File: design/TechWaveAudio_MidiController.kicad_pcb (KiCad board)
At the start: 2 copper layers, 111.5 x 128.5 mm, 92 parts, among them J1 Control, J10 Midi, J12 PiPico2, J13 Velocity, J14 Note, J2 PowerBus, J3 Aux, J4 Gate, J5 Clock, J6 Trigger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

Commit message: working production hardware
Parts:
- moved R25 6.33 mm to (107.9, 37.0)
- moved C11 5.06 mm to (116.8, 41.9), turned to 0 degrees
- moved U6 2.92 mm to (114.1, 40.3)
- moved C8 2.78 mm to (107.8, 44.3), turned to -90 degrees
- moved C10 2.50 mm to (109.5, 42.2)
- moved R24 2.31 mm to (106.7, 37.0), turned to -90 degrees
- moved C9 1.71 mm to (114.6, 44.3), turned to -90 degrees
- moved U5 0.97 mm to (107.0, 40.3)
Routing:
- net GND: track 193.6 -> 214.7 mm, vias 11 -> 8
- net +5V: track 224.6 -> 218.3 mm, vias 4 -> 5
- net /velDAC: track 12.1 -> 15.3 mm
- net /4725Data: track 20.8 -> 22.4 mm
- net /4725Clk: track 23.5 -> 25.0 mm

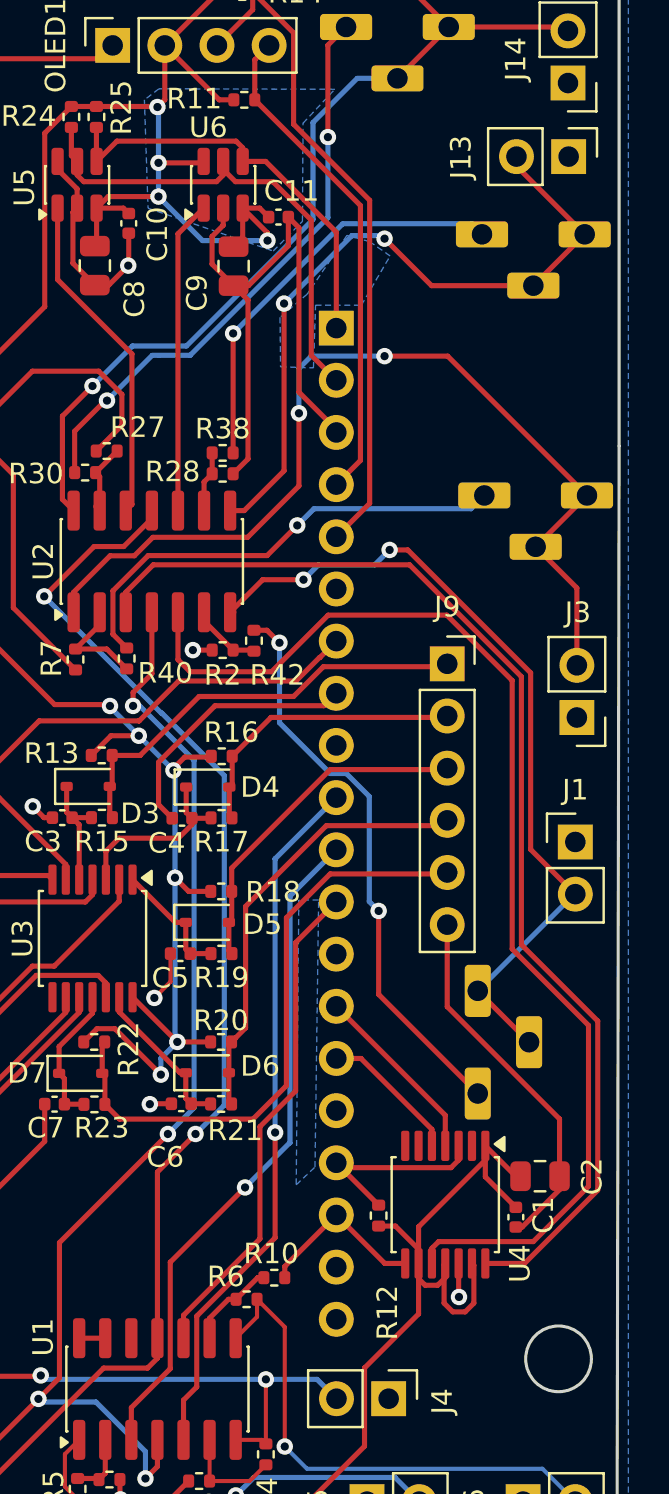
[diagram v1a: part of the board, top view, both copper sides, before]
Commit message: correct i2c / spi
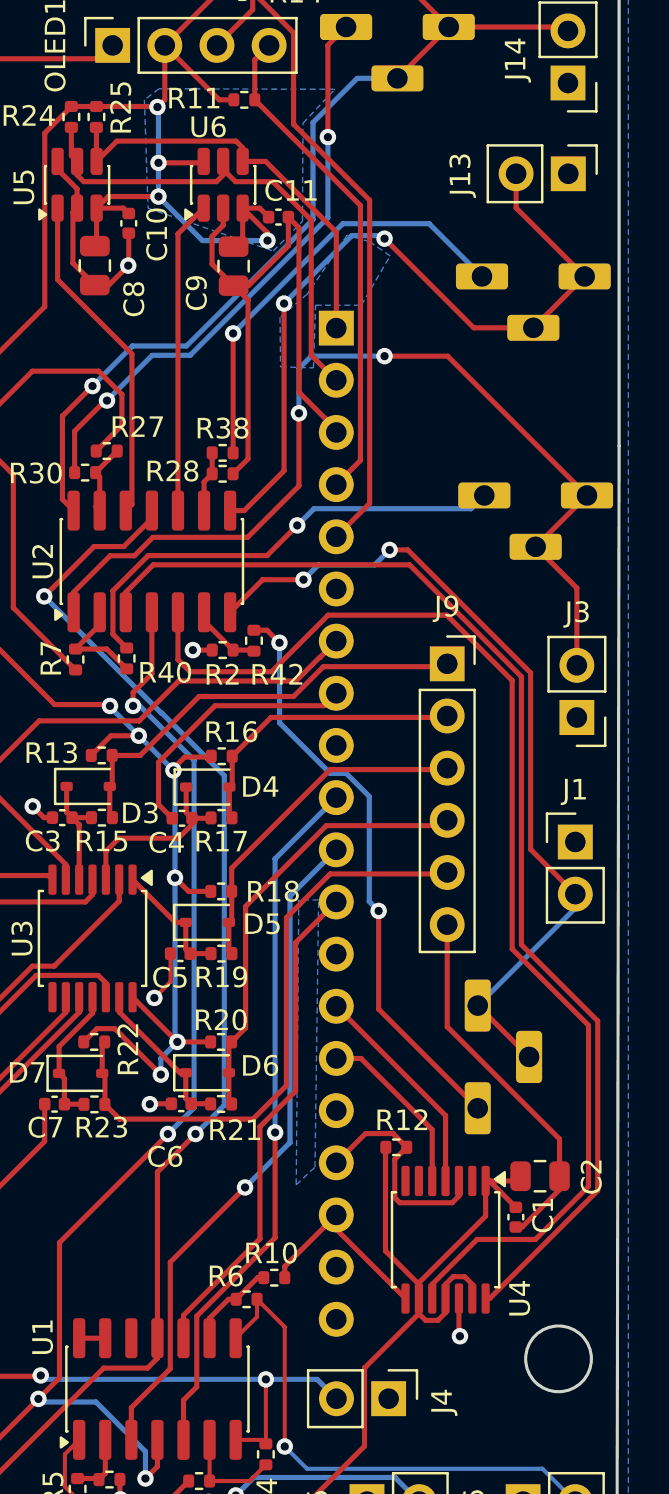
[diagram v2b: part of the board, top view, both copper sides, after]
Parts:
- moved R12 3.43 mm to (122.5, 87.2), turned to 180 degrees
- moved R39 2.05 mm to (129.2, 46.8)
- moved U4 1.71 mm to (124.9, 91.7)
- moved J13 0.84 mm to (130.9, 39.8)
- moved R43 0.72 mm to (128.5, 82.8)
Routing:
- net +5V: track 218.3 -> 216.1 mm
- net /velOut: track 34.8 -> 36.9 mm
- net /4902Clk: track 8.99 -> 10.7 mm
- net /4902Data: track 6.89 -> 8.60 mm
- net /4902CS: track 9.81 -> 11.4 mm
- net GND: track 214.7 -> 216.1 mm
- net Net-(R38-Pad2): track 20.4 -> 21.2 mm
- net /ctlOut: track 40.5 -> 41.2 mm
- net Net-(R42-Pad2): track 27.9 -> 28.7 mm
- net /auxDACOut: track 56.5 -> 57.2 mm
- net /ctlDACOut: track 57.1 -> 57.7 mm

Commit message: working multicore
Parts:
- moved R22 2.15 mm to (109.3, 83.6), turned to -90 degrees
- moved R14 0.39 mm to (114.7, 31.2)
- turned R27 to 180 degrees
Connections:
- SW1 pad 2: unconnected-(SW1-Pad2) -> Net-(D2-A)
- SW1 pad 3: Net-(D2-A) -> unconnected-(SW1-Pad3)
- SW1 pad 6: noteOut -> unconnected-(SW1-Pad6)
- SW1 pad 7: unconnected-(SW1-Pad7) -> noteOut
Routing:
- net GND: track 216.1 -> 260.5 mm, vias 8 -> 4
- net 3.3vSource: track 71.3 -> 67.4 mm
- net +5V: track 216.1 -> 213.4 mm
- net noteOut: track 125.9 -> 123.4 mm, vias 2 -> 1
- net Net-(D2-A): track 16.7 -> 15.7 mm
- net /trgOut: track 25.3 -> 24.6 mm
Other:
- outline, holes or cut-outs redrawn
- board text removed: "DOUBLECHECK"

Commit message: PCB update; cleanups
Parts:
- added C21: 10uF, Capacitor_SMD:C_0805_2012Metric, F.Cu at (110.5, 64.3)
- added C22: 100nf, Capacitor_SMD:C_0402_1005Metric, F.Cu at (107.3, 65.0)
- added C23: 100nf, Capacitor_SMD:C_0402_1005Metric, F.Cu at (112.0, 102.0)
- added C24: 10uF, Capacitor_SMD:C_0805_2012Metric, F.Cu at (111.2, 103.6)
- R37, R39, R41, R43: footprint Resistor_THT:Bourns 3306P-1-102 Trimmer Resistor -> Potentiometer_THT:Potentiometer_Piher_PT-10-V10_Vertical
- moved R37 35.6 mm to (87.7, 41.8), turned to 90 degrees
- moved J5 15.7 mm to (106.0, 108.6), turned to 180 degrees
- moved R39 14.0 mm to (126.3, 33.1), turned to -90 degrees
- moved R41 10.5 mm to (129.9, 47.0), turned to -90 degrees
- moved J6 8.85 mm to (119.8, 104.3)
- moved J4 7.99 mm to (128.4, 104.3), turned to 90 degrees
- moved C2 3.93 mm to (128.8, 92.5)
- moved R43 3.82 mm to (130.3, 79.5), turned to -90 degrees
- moved U4 3.26 mm to (124.2, 94.9)
- moved C1 2.86 mm to (125.5, 89.9), turned to 90 degrees
- moved R12 2.03 mm to (122.4, 89.2)
- moved R8 1.95 mm to (114.2, 102.0)
- moved R5 1.45 mm to (106.9, 102.4)
- moved R4 1.45 mm to (116.1, 100.7)
- moved R10 1.45 mm to (116.5, 92.1)
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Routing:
- net GND: track 260.5 -> 277.8 mm
- net /clkOut: track 21.6 -> 7.03 mm, vias 1 -> 0
- net gateOut: track 42.1 -> 55.8 mm
- net /trgOut: track 24.6 -> 15.1 mm
- net /ctlOut: track 41.2 -> 49.8 mm
- net Net-(R40-Pad2): track 23.1 -> 29.6 mm, vias 1 -> 2
- net +12V: track 97.4 -> 102.5 mm
- net noteOut: track 123.4 -> 119.0 mm
- net /ctlDACOut: track 57.7 -> 62.0 mm
- net /auxDACOut: track 57.2 -> 61.5 mm
- net +5V: track 213.4 -> 209.2 mm
- net Net-(R38-Pad2): track 21.2 -> 25.2 mm, vias 1 -> 2
- net 3.3vSource: track 67.4 -> 70.3 mm, vias 6 -> 7
- net /4902Data: track 8.60 -> 11.5 mm
- net /4902Clk: track 10.7 -> 13.6 mm
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
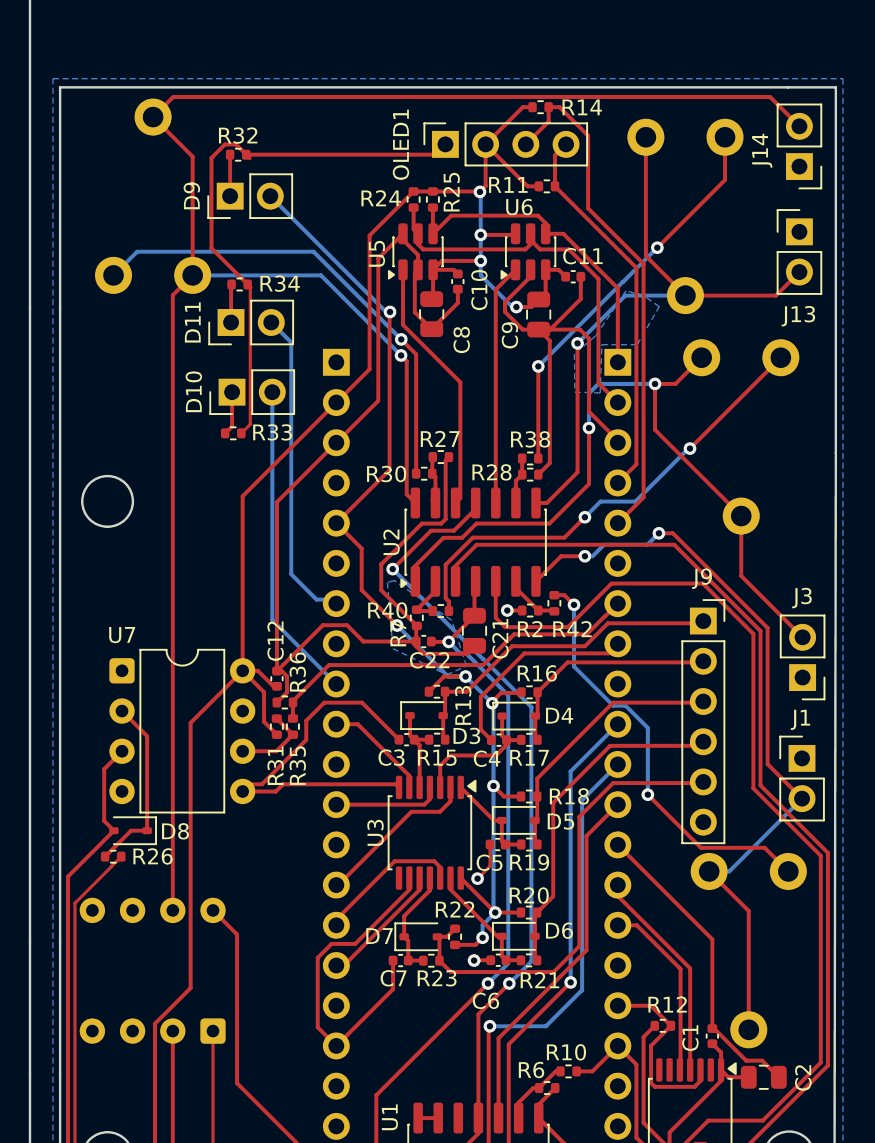
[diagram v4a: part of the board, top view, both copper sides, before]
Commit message: doc cleanups and add images
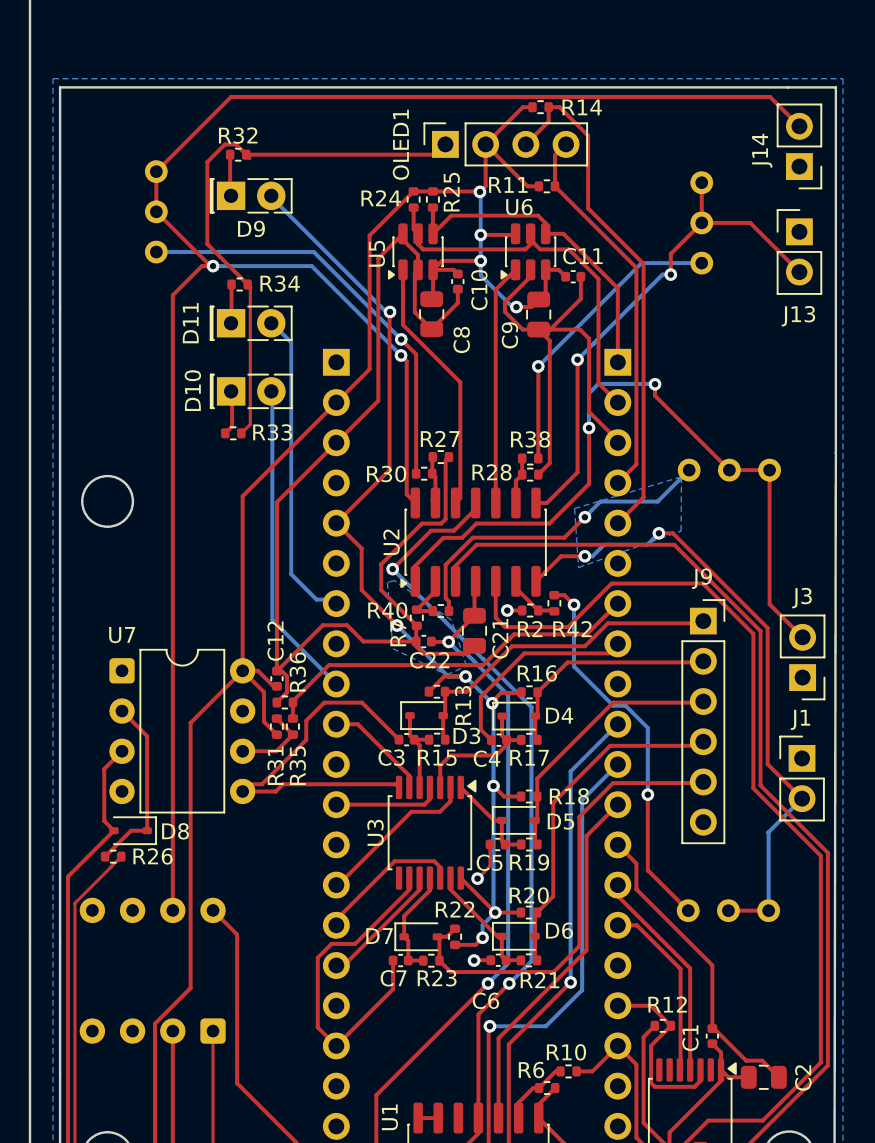
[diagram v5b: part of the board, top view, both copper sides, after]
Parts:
- D10, D11, D9: footprint Connector_PinHeader_2.54mm:PinHeader_1x02_P2.54mm_Vertical -> LED_THT:LED_Rectangular_W5.0mm_H2.0mm
- R37, R39, R41, R43: footprint Potentiometer_THT:Potentiometer_Piher_PT-10-V10_Vertical -> Potentiometer_THT:Potentiometer_Bourns_3296X_Horizontal
- moved R41 9.16 mm to (124.1, 54.1), turned to 180 degrees
- moved R39 8.08 mm to (124.9, 41.0)
- moved R43 6.79 mm to (124.0, 82.0), turned to 180 degrees
- moved R37 3.08 mm to (90.4, 40.4), turned to -90 degrees
- moved D10 0.08 mm to (95.2, 49.1), turned to 0 degrees
- moved D9 0.06 mm to (95.2, 36.8), turned to 0 degrees
- moved D11 0.05 mm to (95.2, 44.9), turned to 0 degrees
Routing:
- net Net-(R40-Pad2): track 29.6 -> 20.9 mm, vias 2 -> 1
- net /ctlOut: track 49.8 -> 41.5 mm
- net Net-(R38-Pad2): track 25.2 -> 18.8 mm, vias 2 -> 1
- net /velOut: track 38.5 -> 32.7 mm, vias 1 -> 2
- net Net-(R30-Pad2): track 30.0 -> 26.7 mm
- net Net-(R42-Pad2): track 26.8 -> 24.3 mm
- net /auxOut: track 47.7 -> 45.6 mm
- net noteOut: track 119.0 -> 117.2 mm, vias 1 -> 2
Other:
- board text added: "v. 1.1.0"
- board text removed: "v. 1.0.0"

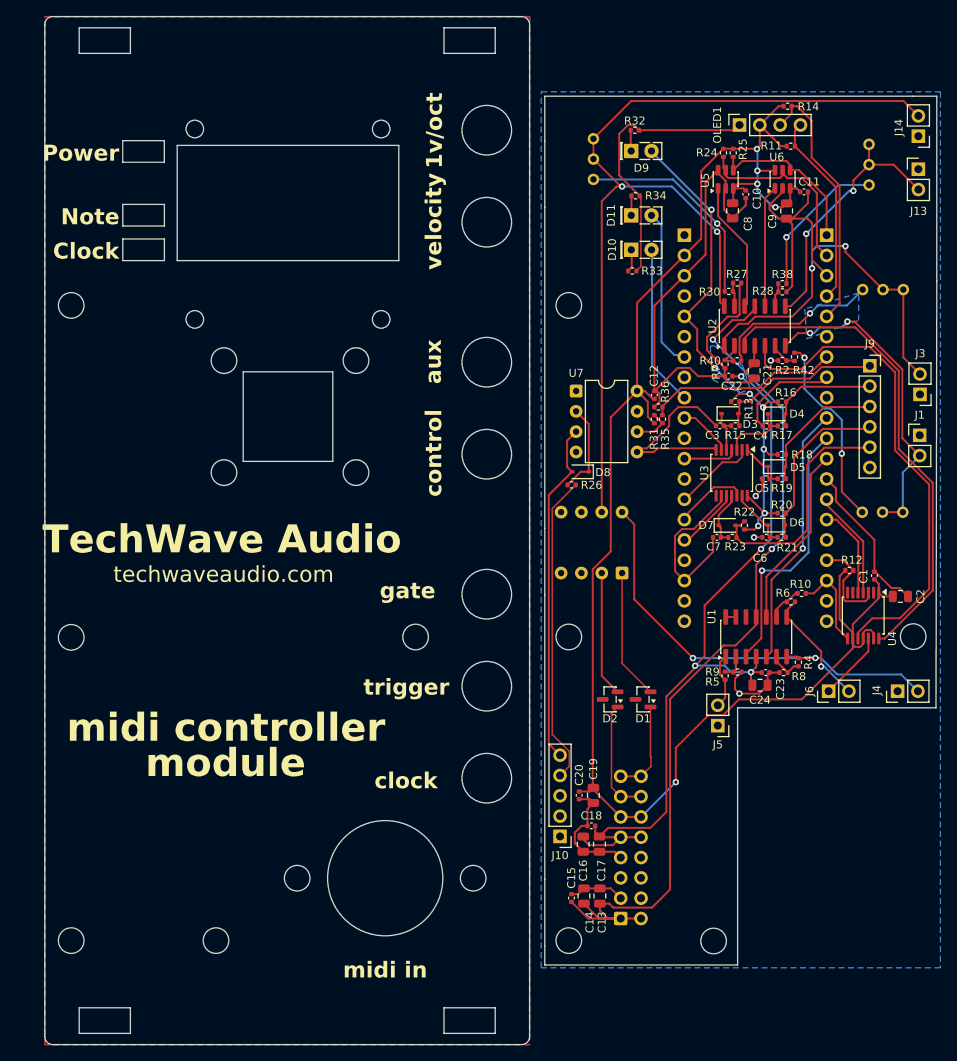
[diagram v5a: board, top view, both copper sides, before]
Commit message: update pcb; move LEDs and mounting
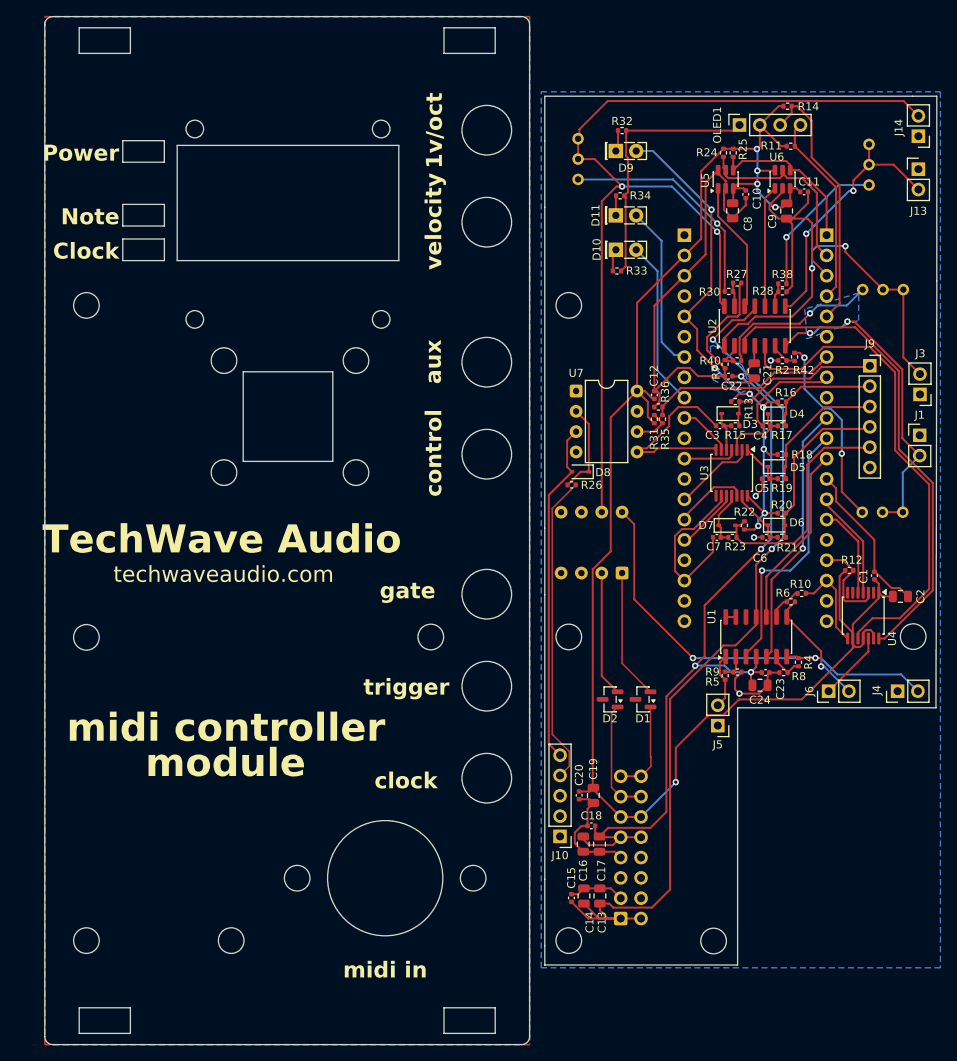
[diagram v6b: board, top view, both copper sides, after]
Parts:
- moved D10 1.92 mm to (93.2, 49.1)
- moved D11 1.92 mm to (93.2, 44.9)
- moved D9 1.92 mm to (93.2, 36.8)
- moved R33 1.92 mm to (93.4, 51.8)
- moved R34 1.92 mm to (93.8, 42.4)
- moved R37 1.92 mm to (88.5, 40.4)
- moved R32 1.59 mm to (94.0, 34.2)
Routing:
- net noteOut: track 117.2 -> 121.8 mm
- net GND: track 278.0 -> 275.2 mm
- net 3.3vSource: track 70.3 -> 72.4 mm
- net Net-(R30-Pad2): track 26.7 -> 28.6 mm
- net /clockLED: track 20.1 -> 21.0 mm
- net /noteLED: track 20.0 -> 20.8 mm
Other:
- outline, holes or cut-outs redrawn

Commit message: hardware docs; cleanups and comments
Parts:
- moved J5 13.7 mm to (118.9, 104.3), turned to -90 degrees
- moved C15 10.8 mm to (97.2, 135.3), turned to 90 degrees
- moved C14 8.85 mm to (95.6, 136.1), turned to 90 degrees
- moved R25 7.82 mm to (115.7, 37.5), turned to 180 degrees
- moved C13 6.53 mm to (93.4, 136.1), turned to 90 degrees
- moved R18 4.06 mm to (114.0, 78.8)
- moved J6 3.97 mm to (123.8, 104.3)
- moved C10 3.19 mm to (111.1, 45.0)
- moved C5 3.08 mm to (112.6, 74.8)
- moved J4 2.68 mm to (131.1, 104.3), turned to 180 degrees
- moved R24 2.59 mm to (109.3, 37.0)
- moved R13 2.50 mm to (109.8, 70.0), turned to -90 degrees
- moved U5 2.32 mm to (109.3, 40.4)
- moved R14 2.30 mm to (112.4, 31.2)
- moved C24 2.13 mm to (109.1, 103.5), turned to 180 degrees
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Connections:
- U1 pad 12: unconnected-(U1D-+-Pad12) -> GND
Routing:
- net -12V: track 115.2 -> 102.8 mm
- net +5V: track 209.2 -> 217.4 mm, vias 5 -> 4
- net /clkOut: track 7.03 -> 14.7 mm
- net +12V: track 102.5 -> 96.6 mm
- net /inBtnDown: track 14.4 -> 17.7 mm
- net /trgOut: track 15.1 -> 17.9 mm
- net Net-(J7-Pin_4): track 24.3 -> 27.1 mm
- net /ctlOut: track 41.5 -> 39.0 mm
- net GND: track 275.2 -> 272.9 mm, vias 4 -> 5
- net /clk: track 33.5 -> 31.6 mm
- net Net-(D3-K): track 5.73 -> 7.12 mm
- net /4725Data: track 22.6 -> 21.3 mm
- net Net-(R30-Pad2): track 28.6 -> 29.9 mm
- net Net-(D5-K): track 6.07 -> 7.32 mm
- net /inBtnBack: track 16.8 -> 17.8 mm
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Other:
- board text added: "(c) 2026 TechWave Audio"
